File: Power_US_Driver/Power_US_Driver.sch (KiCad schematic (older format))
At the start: 1 part, among them J1 Conn_01x03

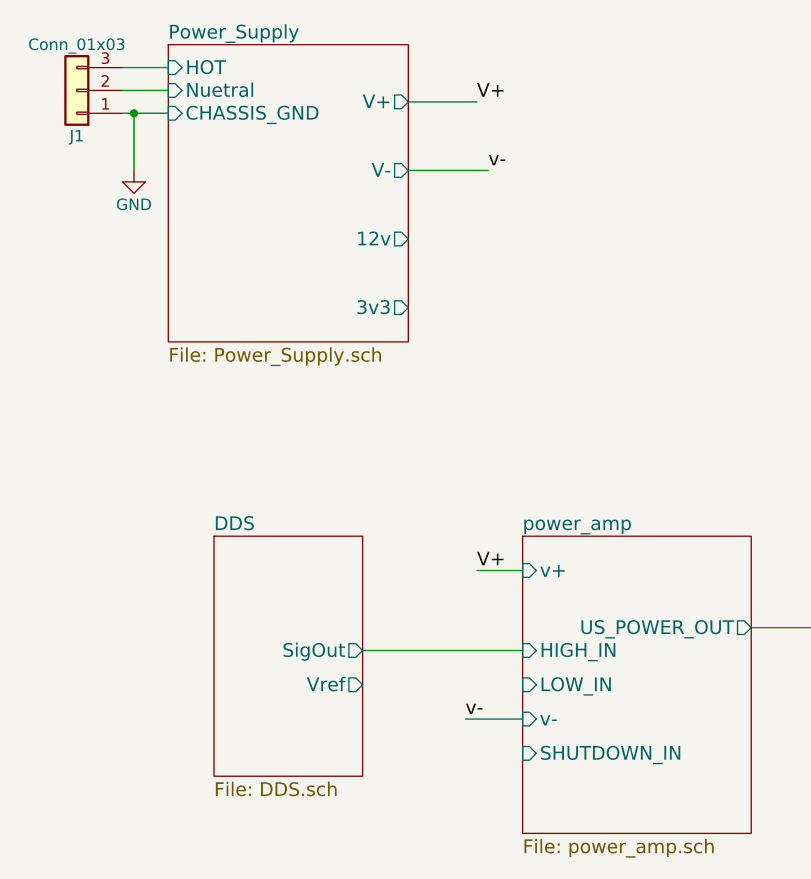
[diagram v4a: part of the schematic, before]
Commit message: Added grounding scheme initial
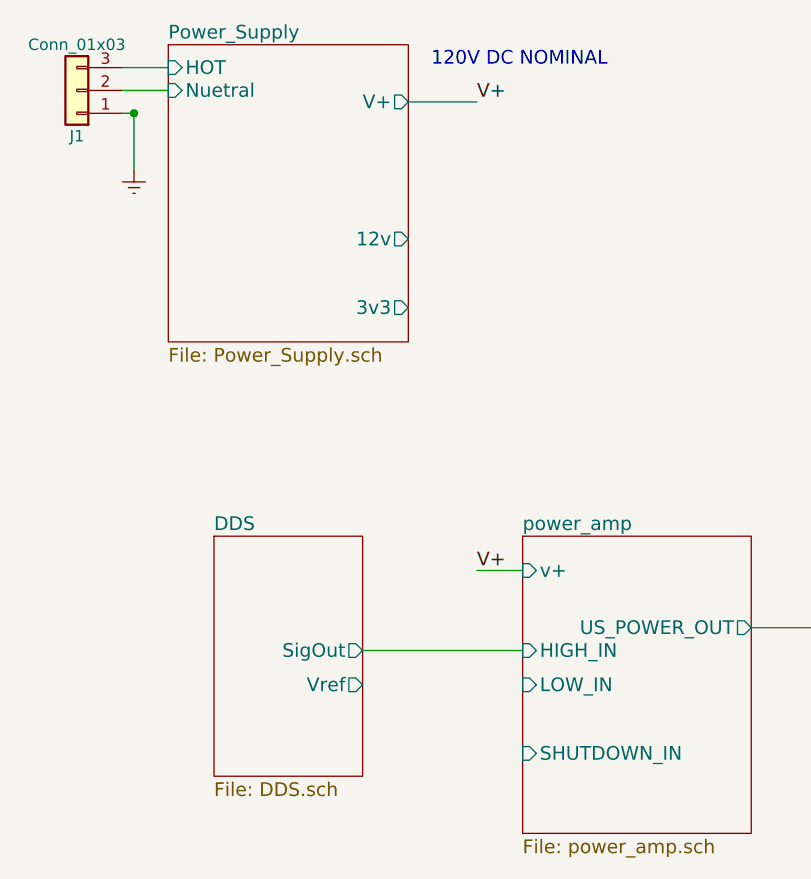
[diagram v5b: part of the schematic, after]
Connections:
- net GND renamed Earth
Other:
- note added: "120V DC NOMINAL"
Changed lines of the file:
@@
 F1 "Power_Supply.sch" 60
 F2 "V+" O R 3350 2700 60
-F3 "V-" O R 3350 3000 60
-F4 "HOT" I L 2300 2550 60
-F5 "Nuetral" I L 2300 2650 60
-F6 "CHASSIS_GND" I L 2300 2750 60
-F7 "12v" O R 3350 3300 60
-F8 "3v3" O R 3350 3600 60
+F3 "HOT" I L 2300 2550 60
+F4 "Nuetral" I L 2300 2650 60
+F5 "12v" O R 3350 3300 60
+F6 "3v3" O R 3350 3600 60
 $EndSheet
 $Sheet
@@
 F1 "power_amp.sch" 60
 F2 "v+" I L 3850 4750 60
-F3 "v-" I L 3850 5400 60
-F4 "US_POWER_OUT" O R 4850 5000 60
-F5 "HIGH_IN" I L 3850 5100 60
-F6 "LOW_IN" I L 3850 5250 60
-F7 "SHUTDOWN_IN" I L 3850 5550 60
+F3 "US_POWER_OUT" O R 4850 5000 60
+F4 "HIGH_IN" I L 3850 5100 60
+F5 "LOW_IN" I L 3850 5250 60
+F6 "SHUTDOWN_IN" I L 3850 5550 60
 $EndSheet
 $Comp
@@
 Text Label 3650 2700 0    60   ~ 0
 V+
-Text Label 3700 3000 0    60   ~ 0
-v-
 Wire Wire Line
 	3650 2700 3350 2700
 Text Label 3650 4750 0    60   ~ 0
 V+
-Wire Wire Line
-	3700 3000 3350 3000
-Text Label 3600 5400 0    60   ~ 0
-v-
-Wire Wire Line
-	3850 5400 3600 5400
 Wire Wire Line
 	3650 4750 3850 4750
@@
 	2100 2650 2300 2650
 Wire Wire Line
-	2100 2750 2300 2750
+	2150 3000 2150 2750
+Connection ~ 2150 2750
+Wire Wire Line
+	5350 5000 4850 5000
 $Comp
-L GND #PWR1
-U 1 1 5AAE997E
+L Earth #PWR?
+U 1 1 5AB015D4
 P 2150 3000
-F 0 "#PWR1" H 2150 2750 50  0001 C CNN
-F 1 "GND" H 2150 2850 50  0000 C CNN
+F 0 "#PWR?" H 2150 2750 50  0001 C CNN
+F 1 "Earth" H 2150 2850 50  0001 C CNN
 F 2 "" H 2150 3000 50  0001 C CNN
 F 3 "" H 2150 3000 50  0001 C CNN
@@
 $EndComp
 Wire Wire Line
-	2150 3000 2150 2750
-Connection ~ 2150 2750
-Wire Wire Line
-	5350 5000 4850 5000
+	2150 2750 2100 2750
+Text Notes 3450 2550 0    60   ~ 0
+120V DC NOMINAL
 $EndSCHEMATC

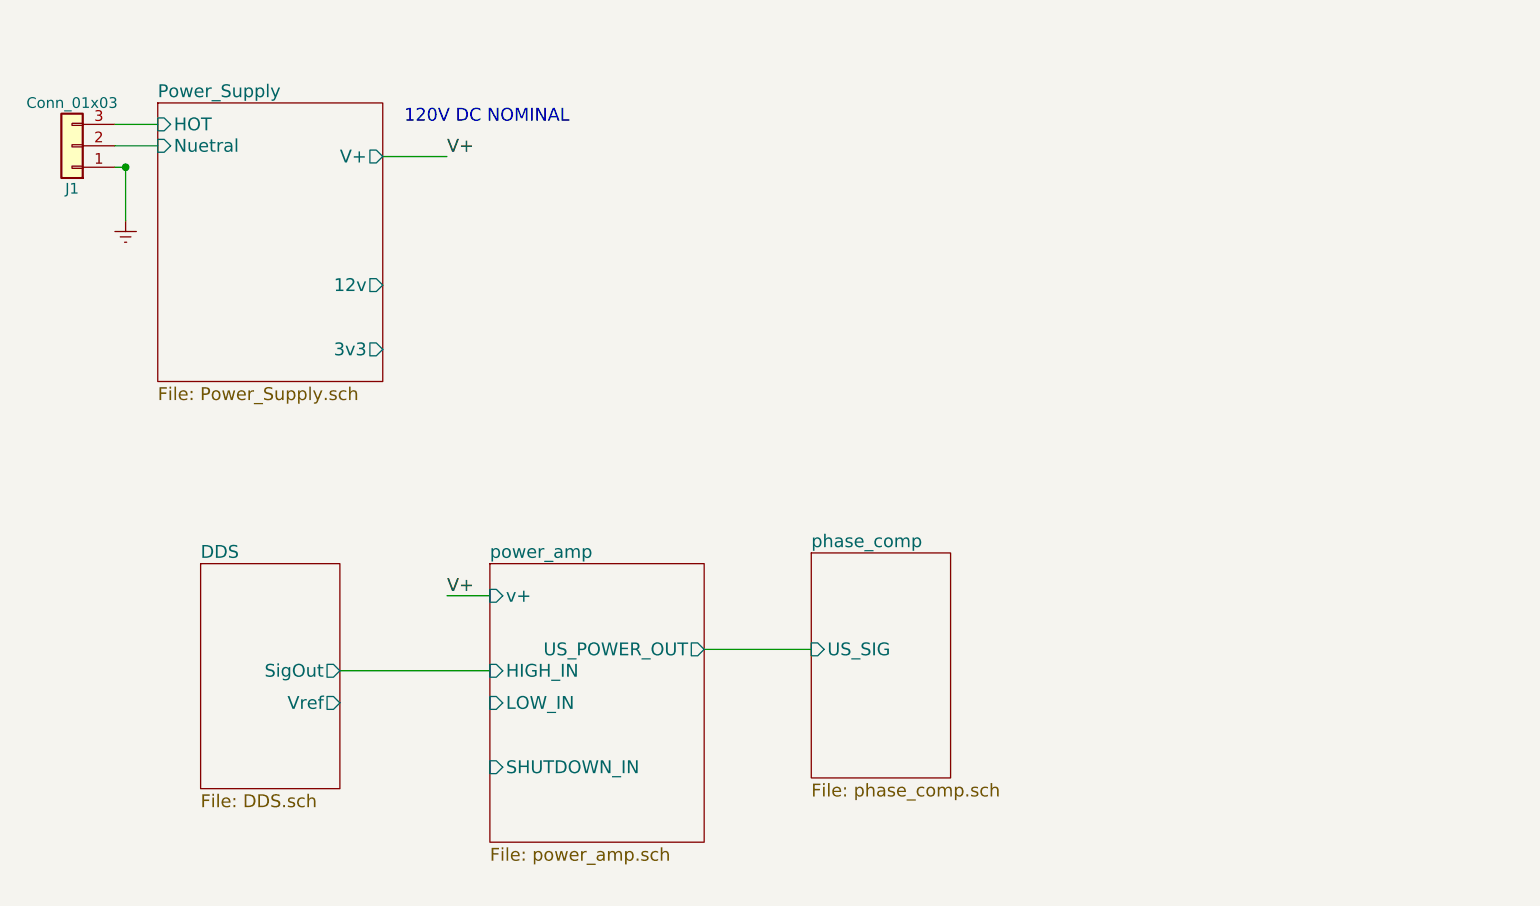
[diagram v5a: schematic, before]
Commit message: CURRENT SENSE REROUT, HIGHSIDE DRIVER GROUNDING
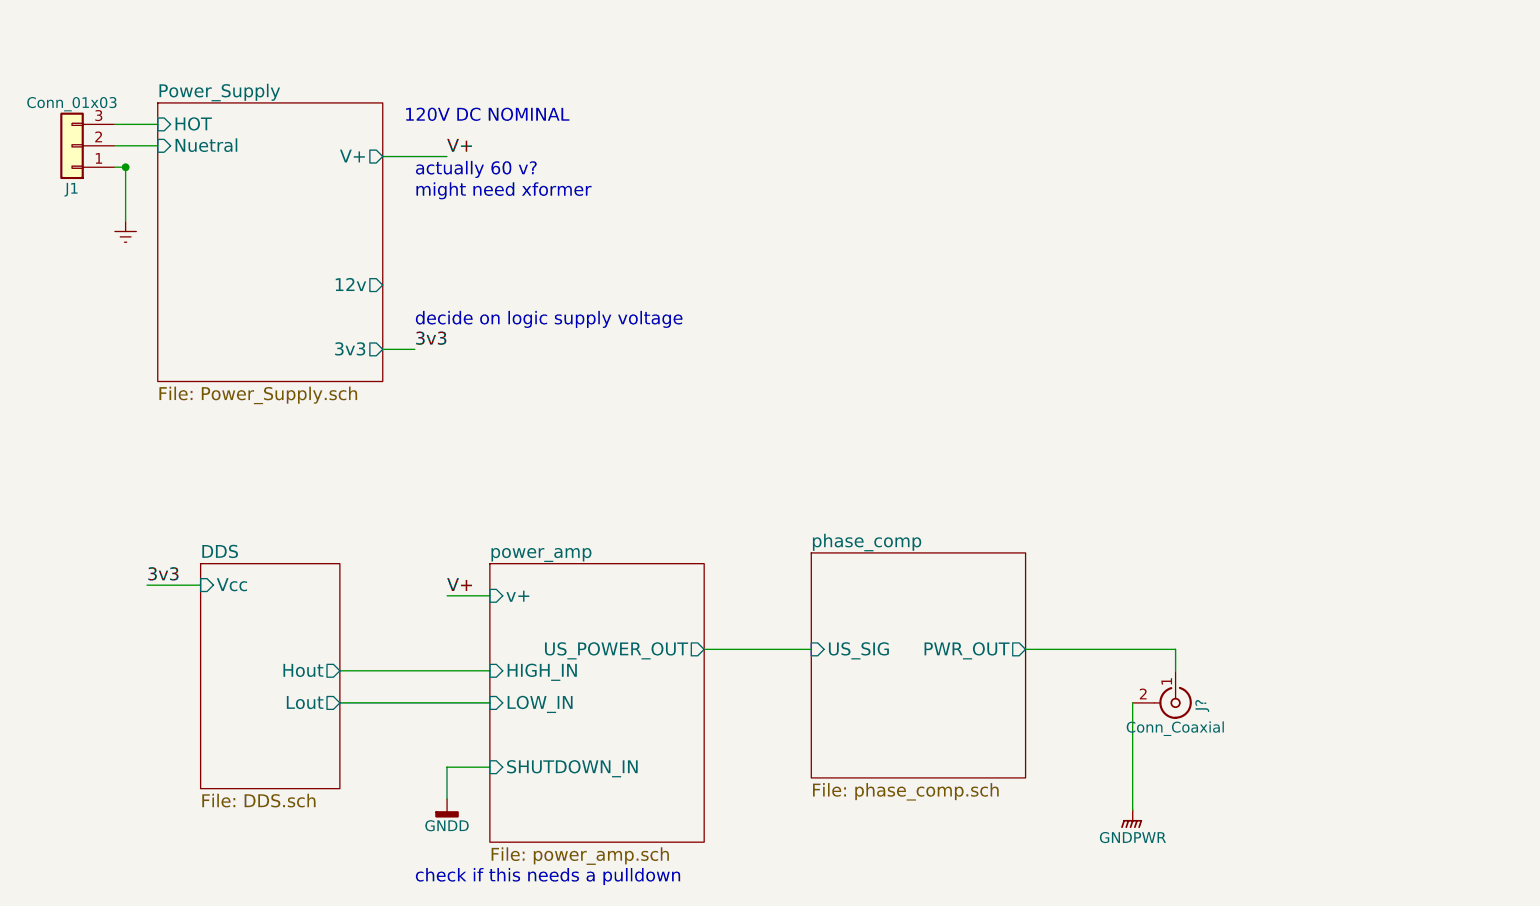
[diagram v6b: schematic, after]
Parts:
- added J?: Conn_Coaxial, symbol Conn_Coaxial
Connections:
- new net GNDPWR: J?.2 (Ext)
- new net phase_comp/PWR_OUT: J?.1 (In)
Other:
- note added: "actually 60 v?"
- note added: "check if this needs a pulldown"
- note added: "decide on logic supply voltage"
- note added: "might need xformer"
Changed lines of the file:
@@
 LIBS:LIA-cache
 LIBS:power_US
+LIBS:JasMoH_Parts
 LIBS:Power_US_Driver-cache
 EELAYER 25 0
@@
 F0 "DDS" 60
 F1 "DDS.sch" 60
-F2 "SigOut" O R 3150 5100 60
-F3 "Vref" O R 3150 5250 60
+F2 "Vcc" I L 2500 4700 60
+F3 "Hout" O R 3150 5100 60
+F4 "Lout" O R 3150 5250 60
 $EndSheet
 $Sheet
-S 5350 4550 650  1050
+S 5350 4550 1000 1050
 U 5AAD908C
 F0 "phase_comp" 60
 F1 "phase_comp.sch" 60
 F2 "US_SIG" I L 5350 5000 60
+F3 "PWR_OUT" O R 6350 5000 60
 $EndSheet
 $Sheet
@@
 	5350 5000 4850 5000
 $Comp
-L Earth #PWR?
+L Earth #PWR1
 U 1 1 5AB015D4
 P 2150 3000
-F 0 "#PWR?" H 2150 2750 50  0001 C CNN
+F 0 "#PWR1" H 2150 2750 50  0001 C CNN
 F 1 "Earth" H 2150 2850 50  0001 C CNN
 F 2 "" H 2150 3000 50  0001 C CNN
@@
 Text Notes 3450 2550 0    60   ~ 0
 120V DC NOMINAL
+Wire Wire Line
+	3150 5250 3850 5250
+Text Notes 3500 2800 0    60   ~ 0
+actually 60 v?
+Text Notes 3500 2900 0    60   ~ 0
+might need xformer
+Text Notes 3500 3500 0    60   ~ 0
+decide on logic supply voltage
+Wire Wire Line
+	2250 4700 2500 4700
+Text Label 2250 4700 0    60   ~ 0
+3v3
+Text Label 3500 3600 0    60   ~ 0
+3v3
+Wire Wire Line
+	3500 3600 3350 3600
+$Comp
+L GNDD #PWR?
+U 1 1 5AB1DC44
+P 3650 5700
+F 0 "#PWR?" H 3650 5450 50  0001 C CNN
+F 1 "GNDD" H 3650 5575 50  0000 C CNN
+F 2 "" H 3650 5700 50  0001 C CNN
+F 3 "" H 3650 5700 50  0001 C CNN
+	1    3650 5700
+	1    0    0    -1
+$EndComp
+Wire Wire Line
+	3850 5550 3650 5550
+Wire Wire Line
+	3650 5550 3650 5700
+Text Notes 3500 6100 0    60   ~ 0
+check if this needs a pulldown
+$Comp
+L Conn_Coaxial J?
+U 1 1 5AB1E9D0
+P 7050 5250
+F 0 "J?" H 7060 5370 50  0000 C CNN
+F 1 "Conn_Coaxial" V 7165 5250 50  0000 C CNN
+F 2 "" H 7050 5250 50  0001 C CNN
+F 3 "" H 7050 5250 50  0001 C CNN
+	1    7050 5250
+	0    1    1    0
+$EndComp
+Wire Wire Line
+	6850 5750 6850 5250
+Wire Wire Line
+	7050 5000 7050 5100
+$Comp
+L GNDPWR #PWR?
+U 1 1 5AB1E9D9
+P 6850 5750
+F 0 "#PWR?" H 6850 5550 50  0001 C CNN
+F 1 "GNDPWR" H 6850 5620 50  0000 C CNN
+F 2 "" H 6850 5700 50  0001 C CNN
+F 3 "" H 6850 5700 50  0001 C CNN
+	1    6850 5750
+	1    0    0    -1
+$EndComp
+Wire Wire Line
+	6350 5000 7050 5000
 $EndSCHEMATC

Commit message: initial Current sense more vacilating over power drive solution
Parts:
- gave numbers to parts that had none: 1
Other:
- note added: "drive topology options:\nfull wave reactify, half bridge\ntwo half wave reactify, +- fets\nPWR OP AMP"
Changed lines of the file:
@@
 F5 "12v" O R 3350 3300 60
 F6 "3v3" O R 3350 3600 60
+F7 "V-" O R 3350 3100 60
 $EndSheet
 $Sheet
@@
 F5 "LOW_IN" I L 3850 5250 60
 F6 "SHUTDOWN_IN" I L 3850 5550 60
+F7 "logic_pwr" I L 3850 4850 60
+F8 "V-" I L 3850 5400 60
 $EndSheet
 $Comp
@@
 	3500 3600 3350 3600
 $Comp
-L GNDD #PWR?
+L GNDD #PWR2
 U 1 1 5AB1DC44
 P 3650 5700
-F 0 "#PWR?" H 3650 5450 50  0001 C CNN
+F 0 "#PWR2" H 3650 5450 50  0001 C CNN
 F 1 "GNDD" H 3650 5575 50  0000 C CNN
 F 2 "" H 3650 5700 50  0001 C CNN
@@
 check if this needs a pulldown
 $Comp
-L Conn_Coaxial J?
+L Conn_Coaxial J2
 U 1 1 5AB1E9D0
 P 7050 5250
-F 0 "J?" H 7060 5370 50  0000 C CNN
+F 0 "J2" H 7060 5370 50  0000 C CNN
 F 1 "Conn_Coaxial" V 7165 5250 50  0000 C CNN
 F 2 "" H 7050 5250 50  0001 C CNN
@@
 	7050 5000 7050 5100
 $Comp
-L GNDPWR #PWR?
+L GNDPWR #PWR3
 U 1 1 5AB1E9D9
 P 6850 5750
-F 0 "#PWR?" H 6850 5550 50  0001 C CNN
+F 0 "#PWR3" H 6850 5550 50  0001 C CNN
 F 1 "GNDPWR" H 6850 5620 50  0000 C CNN
 F 2 "" H 6850 5700 50  0001 C CNN
@@
 Wire Wire Line
 	6350 5000 7050 5000
+Text Label 3700 3100 0    60   ~ 0
+V-
+Wire Wire Line
+	3700 3100 3350 3100
+Text Label 3650 5400 0    60   ~ 0
+V-
+Wire Wire Line
+	3650 5400 3850 5400
+Text Label 3650 4850 0    60   ~ 0
+3v3
+Wire Wire Line
+	3650 4850 3850 4850
+Text Notes 5600 3650 0    60   ~ 0
+drive topology options:\nfull wave reactify, half bridge\ntwo half wave reactify, +- fets\nPWR OP AMP
 $EndSCHEMATC

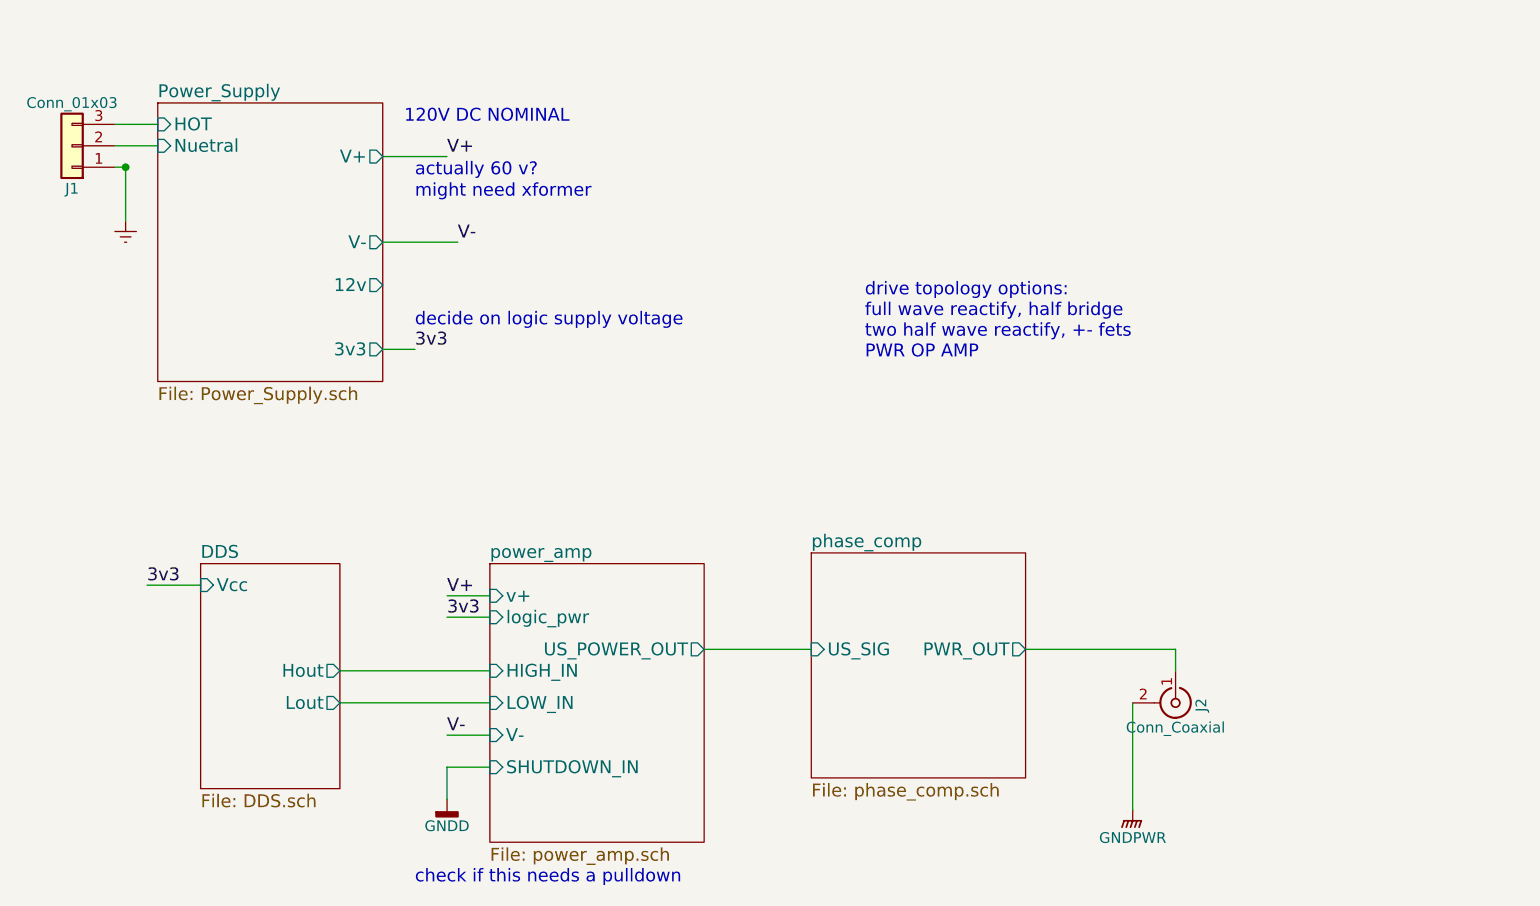
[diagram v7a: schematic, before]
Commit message: Screw it, 0-120V output voltage is fine for a cheapo first pass
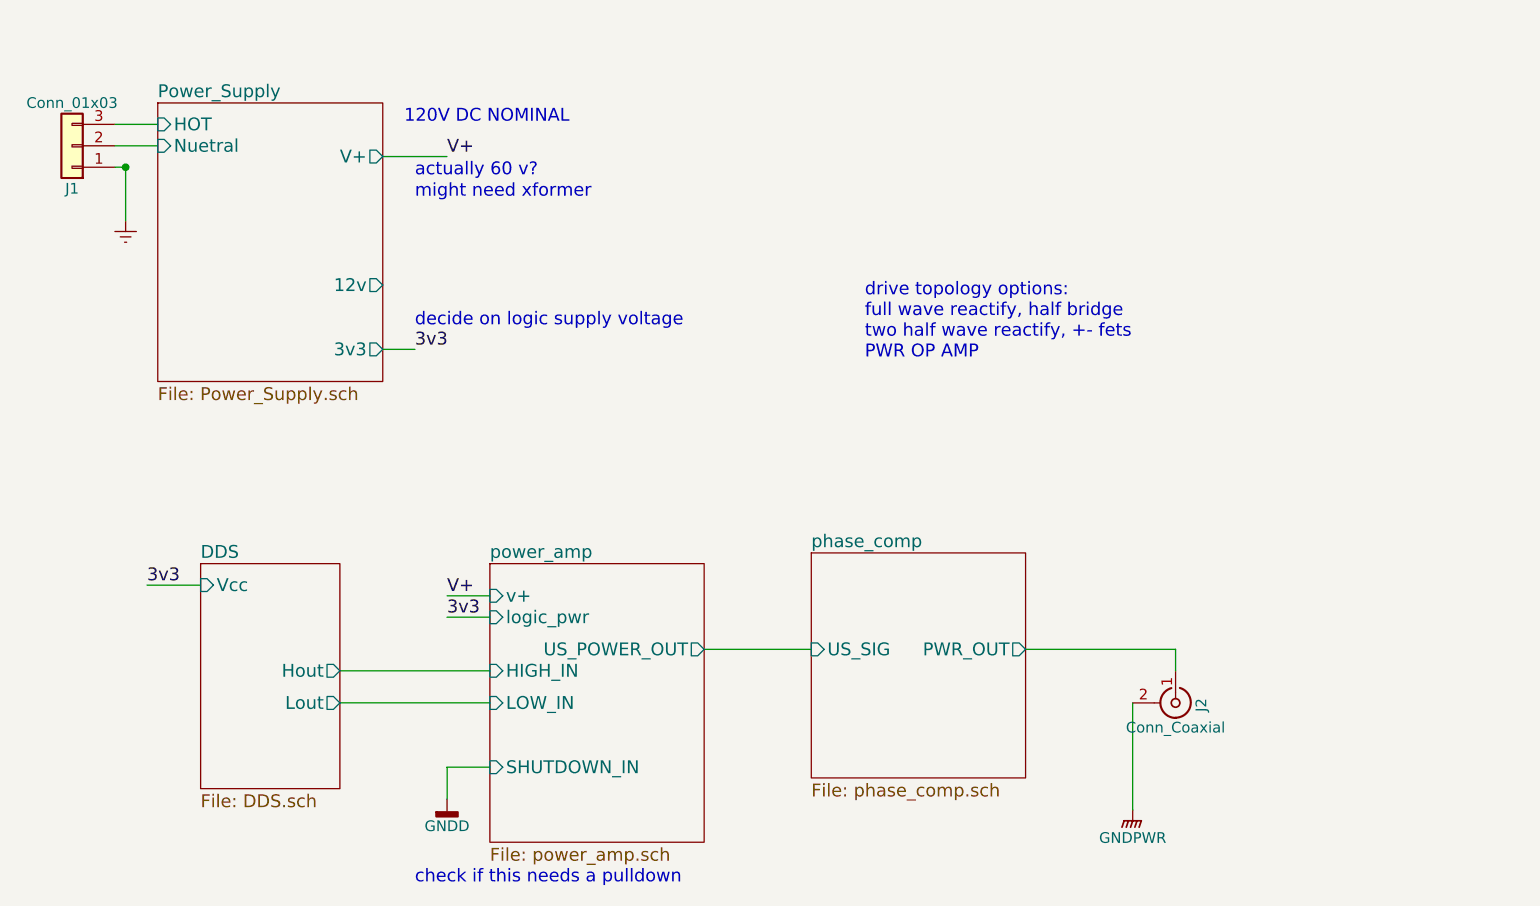
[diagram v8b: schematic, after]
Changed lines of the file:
@@
 F5 "12v" O R 3350 3300 60
 F6 "3v3" O R 3350 3600 60
-F7 "V-" O R 3350 3100 60
 $EndSheet
 $Sheet
@@
 F2 "US_SIG" I L 5350 5000 60
 F3 "PWR_OUT" O R 6350 5000 60
-$EndSheet
-$Sheet
-S 3850 4600 1000 1300
-U 5AAD9099
-F0 "power_amp" 60
-F1 "power_amp.sch" 60
-F2 "v+" I L 3850 4750 60
-F3 "US_POWER_OUT" O R 4850 5000 60
-F4 "HIGH_IN" I L 3850 5100 60
-F5 "LOW_IN" I L 3850 5250 60
-F6 "SHUTDOWN_IN" I L 3850 5550 60
-F7 "logic_pwr" I L 3850 4850 60
-F8 "V-" I L 3850 5400 60
 $EndSheet
 $Comp
@@
 Wire Wire Line
 	6350 5000 7050 5000
-Text Label 3700 3100 0    60   ~ 0
-V-
-Wire Wire Line
-	3700 3100 3350 3100
-Text Label 3650 5400 0    60   ~ 0
-V-
-Wire Wire Line
-	3650 5400 3850 5400
 Text Label 3650 4850 0    60   ~ 0
 3v3
@@
 Text Notes 5600 3650 0    60   ~ 0
 drive topology options:\nfull wave reactify, half bridge\ntwo half wave reactify, +- fets\nPWR OP AMP
+$Sheet
+S 3850 4600 1000 1300
+U 5AAD9099
+F0 "power_amp" 60
+F1 "power_amp.sch" 60
+F2 "v+" I L 3850 4750 60
+F3 "US_POWER_OUT" O R 4850 5000 60
+F4 "HIGH_IN" I L 3850 5100 60
+F5 "LOW_IN" I L 3850 5250 60
+F6 "SHUTDOWN_IN" I L 3850 5550 60
+F7 "logic_pwr" I L 3850 4850 60
+$EndSheet
 $EndSCHEMATC
